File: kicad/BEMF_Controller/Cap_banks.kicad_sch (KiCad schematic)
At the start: 63 parts

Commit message: Simplification, high and low side driven together.
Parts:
- C10, C24, C25, C26, C27, C32, C33, C34, C35, C6, C7, C8: footprint main:CPOL-RADIAL-5MM-10MM -> Capacitor_THT:CP_Radial_D10.0mm_P5.00mm; symbol main-eagle-import:1000UF-RADIAL-5MM-25V-20% -> Component_Library:C_Pol_470uF
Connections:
- net CAP_BANK_A+: now also C10.1; no longer C10.+
- net CAP_BANK_B+: now also C27.1; no longer C27.+
- net CAP_BANK_C+: now also C35.1; no longer C35.+
- net SHUNT_A+: now also C8.2; no longer C8.-
- net SHUNT_B+: now also C26.2; no longer C26.-
- net SHUNT_C+: now also C34.2; no longer C34.-
- net at C30.2, D20.1 (A), D20.2 (A)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: now also C27.2; no longer C27.-
- net at C28.1, D24.1 (A), D24.2 (A)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: now also C25.1; no longer C25.+
- net at C31.2, D21.1 (A), D21.2 (A)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: now also C24.2; no longer C24.-
- net at C13.1, D13.1 (A), D13.2 (A)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: now also C6.1; no longer C6.+
- net at C23.2, D13.3 (K), D8.1 (A)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: now also C10.2; no longer C10.-
- net at C22.1, D15.1 (A), D15.2 (A)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: now also C8.1; no longer C8.+
- net at C29.1, D25.1 (A), D25.2 (A)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: now also C26.1; no longer C26.+
- net at C28.2, D22.1 (A), D22.2 (A)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: now also C25.2; no longer C25.-
- net at C36.1, D34.1 (A), D34.2 (A)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: now also C33.1; no longer C33.+
- net at C36.2, D32.1 (A), D32.2 (A)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: now also C33.2; no longer C33.-
- net at C37.1, D35.1 (A), D35.2 (A)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: now also C34.1; no longer C34.+
- net at C21.2, D12.1 (A), D12.2 (A)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: now also C7.2; no longer C7.-
- net at C38.2, D30.1 (A), D30.2 (A)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: now also C35.2; no longer C35.-
- net at C13.2, D10.1 (A), D10.2 (A)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: now also C6.2; no longer C6.-
- net at C31.1, D23.1 (A), D23.2 (A)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: now also C24.1; no longer C24.+
- net at C39.1, D33.1 (A), D33.2 (A)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: now also C32.1; no longer C32.+
- net at C21.1, D14.1 (A), D14.2 (A)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: now also C7.1; no longer C7.+
- net at C39.2, D31.1 (A), D31.2 (A)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: now also C32.2; no longer C32.-

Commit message: Fixed all warnings.
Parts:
- R30, R31, R32: footprint main:R2512 -> Resistor_SMD:R_2512_6332Metric_Pad1.40x3.35mm_HandSolder; symbol main-eagle-import:RESISTOR -> Component_Library:R0005
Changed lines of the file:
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@@
 	)
 	(junction
-		(at 105.41 175.26)
-		(diameter 0)
-		(color 0 0 0 0)
-	)
-	(junction
 		(at 124.46 157.48)
 		(diameter 0)
@@
 	)
 	(junction
+		(at 30.48 185.42)
+		(diameter 0)
+		(color 0 0 0 0)
+	)
+	(junction
 		(at 143.51 115.57)
 		(diameter 0)
@@
 	)
 	(junction
-		(at 105.41 185.42)
+		(at 30.48 175.26)
 		(diameter 0)
 		(color 0 0 0 0)
@@
 	)
 	(junction
+		(at 105.41 175.26)
+		(diameter 0)
+		(color 0 0 0 0)
+	)
+	(junction
 		(at 196.85 127)
 		(diameter 0)
@@
 	)
 	(junction
-		(at 196.85 36.83)
+		(at 182.88 185.42)
 		(diameter 0)
 		(color 0 0 0 0)
 	)
 	(junction
-		(at 182.88 175.26)
+		(at 196.85 36.83)
 		(diameter 0)
 		(color 0 0 0 0)
@@
 	)
 	(junction
-		(at 30.48 185.42)
+		(at 105.41 185.42)
 		(diameter 0)
 		(color 0 0 0 0)
@@
 	)
 	(junction
-		(at 182.88 185.42)
-		(diameter 0)
-		(color 0 0 0 0)
-	)
-	(junction
-		(at 30.48 175.26)
-		(diameter 0)
-		(color 0 0 0 0)
-	)
-	(junction
 		(at 44.45 60.96)
 		(diameter 0)
@@
 	)
 	(junction
+		(at 182.88 175.26)
+		(diameter 0)
+		(color 0 0 0 0)
+	)
+	(junction
 		(at 196.85 99.06)
 		(diameter 0)
@@
 	(wire
 		(pts
-			(xy 182.88 175.26) (xy 191.77 175.26)
-		)
-		(stroke
-			(width 0)
-			(type default)
-		)
-	)
-	(wire
-		(pts
 			(xy 201.93 77.47) (xy 201.93 81.28)
 		)
@@
 	(wire
 		(pts
-			(xy 30.48 175.26) (xy 39.37 175.26)
+			(xy 30.48 175.26) (xy 30.48 176.53)
 		)
 		(stroke
@@
 	(wire
 		(pts
-			(xy 67.31 157.48) (xy 64.77 157.48)
+			(xy 30.48 184.15) (xy 30.48 185.42)
 		)
 		(stroke
@@
 	(wire
 		(pts
-			(xy 30.48 185.42) (xy 38.1 185.42)
+			(xy 67.31 157.48) (xy 64.77 157.48)
 		)
 		(stroke
@@
 	(wire
 		(pts
-			(xy 182.88 185.42) (xy 190.5 185.42)
+			(xy 97.79 26.67) (xy 110.49 26.67)
 		)
 		(stroke
@@
 	(wire
 		(pts
-			(xy 97.79 26.67) (xy 110.49 26.67)
+			(xy 196.85 60.96) (xy 196.85 64.77)
 		)
 		(stroke
@@
 	(wire
 		(pts
-			(xy 196.85 60.96) (xy 196.85 64.77)
+			(xy 31.75 36.83) (xy 44.45 36.83)
 		)
 		(stroke
@@
 	(wire
 		(pts
-			(xy 31.75 36.83) (xy 44.45 36.83)
+			(xy 196.85 115.57) (xy 200.66 115.57)
 		)
 		(stroke
@@
 	(wire
 		(pts
-			(xy 196.85 115.57) (xy 200.66 115.57)
+			(xy 48.26 157.48) (xy 48.26 161.29)
 		)
 		(stroke
@@
 	(wire
 		(pts
-			(xy 48.26 157.48) (xy 48.26 161.29)
+			(xy 125.73 77.47) (xy 125.73 81.28)
 		)
 		(stroke
@@
 	(wire
 		(pts
-			(xy 125.73 77.47) (xy 125.73 81.28)
+			(xy 105.41 175.26) (xy 115.57 175.26)
 		)
 		(stroke
@@
 	(wire
 		(pts
+			(xy 30.48 175.26) (xy 39.37 175.26)
+		)
+		(stroke
+			(width 0)
+			(type default)
+		)
+	)
+	(wire
+		(pts
 			(xy 54.61 157.48) (xy 57.15 157.48)
 		)
@@
 	(wire
 		(pts
-			(xy 182.88 185.42) (xy 171.45 185.42)
+			(xy 171.45 185.42) (xy 182.88 185.42)
 		)
 		(stroke
@@
 	(wire
 		(pts
+			(xy 182.88 175.26) (xy 191.77 175.26)
+		)
+		(stroke
+			(width 0)
+			(type default)
+		)
+	)
+	(wire
+		(pts
 			(xy 173.99 99.06) (xy 181.61 99.06)
 		)
@@
 	(wire
 		(pts
-			(xy 30.48 185.42) (xy 20.32 185.42)
+			(xy 20.32 185.42) (xy 30.48 185.42)
 		)
 		(stroke
@@
 	(wire
 		(pts
+			(xy 105.41 185.42) (xy 113.03 185.42)
+		)
+		(stroke
+			(width 0)
+			(type default)
+		)
+	)
+	(wire
+		(pts
+			(xy 182.88 185.42) (xy 190.5 185.42)
+		)
+		(stroke
+			(width 0)
+			(type default)
+		)
+	)
+	(wire
+		(pts
 			(xy 116.84 41.91) (xy 116.84 48.26)
 		)
@@
 	(wire
 		(pts
+			(xy 105.41 175.26) (xy 105.41 176.53)
+		)
+		(stroke
+			(width 0)
+			(type default)
+		)
+	)
+	(wire
+		(pts
 			(xy 124.46 157.48) (xy 124.46 161.29)
 		)
@@
 	(wire
 		(pts
-			(xy 105.41 175.26) (xy 115.57 175.26)
-		)
-		(stroke
-			(width 0)
-			(type default)
-		)
-	)
-	(wire
-		(pts
 			(xy 97.79 36.83) (xy 100.33 36.83)
 		)
@@
 	(wire
 		(pts
+			(xy 182.88 184.15) (xy 182.88 185.42)
+		)
+		(stroke
+			(width 0)
+			(type default)
+		)
+	)
+	(wire
+		(pts
 			(xy 55.88 36.83) (xy 44.45 36.83)
 		)
@@
 	(wire
 		(pts
+			(xy 182.88 175.26) (xy 182.88 176.53)
+		)
+		(stroke
+			(width 0)
+			(type default)
+		)
+	)
+	(wire
+		(pts
 			(xy 58.42 147.32) (xy 54.61 147.32)
 		)
@@
 	(wire
 		(pts
+			(xy 105.41 184.15) (xy 105.41 185.42)
+		)
+		(stroke
+			(width 0)
+			(type default)
+		)
+	)
+	(wire
+		(pts
 			(xy 120.65 127) (xy 120.65 137.16)
 		)
@@
 	(wire
 		(pts
+			(xy 30.48 185.42) (xy 38.1 185.42)
+		)
+		(stroke
+			(width 0)
+			(type default)
+		)
+	)
+	(wire
+		(pts
 			(xy 120.65 91.44) (xy 120.65 99.06)
 		)
@@
 	(wire
 		(pts
-			(xy 105.41 185.42) (xy 113.03 185.42)
-		)
-		(stroke
-			(width 0)
-			(type default)
-		)
-	)
-	(wire
-		(pts
 			(xy 115.57 115.57) (xy 115.57 119.38)
 		)
@@
 	)
 	(symbol
-		(lib_id "main-eagle-import:RESISTOR")
-		(at 182.88 180.34 270)
+		(lib_id "Component_Library:R0005")
+		(at 182.88 180.34 0)
 		(unit 1)
 		(exclude_from_sim no)
@@
 		(dnp no)
 		(property "Reference" "R32"
-			(at 184.404 180.34 0)
+			(at 178.308 181.102 0)
 			(effects
 				(font
@@
 		)
 		(property "Value" "0.0005"
-			(at 181.356 180.34 0)
+			(at 189.738 179.07 0)
 			(effects
 				(font
@@
 			)
 		)
-		(property "Footprint" "main:R2512"
-			(at 182.88 180.34 0)
+		(property "Footprint" "Resistor_SMD:R_2512_6332Metric_Pad1.40x3.35mm_HandSolder"
+			(at 181.102 180.34 90)
 			(effects
 				(font
@@
 			)
 		)
-		(property "Datasheet" ""
+		(property "Datasheet" "~"
 			(at 182.88 180.34 0)
 			(effects
@@
 			)
 		)
-		(property "Description" ""
+		(property "Description" "Resistor"
 			(at 182.88 180.34 0)
 			(effects
@@
 	)
 	(symbol
-		(lib_id "main-eagle-import:RESISTOR")
-		(at 105.41 180.34 270)
+		(lib_id "Component_Library:R0005")
+		(at 105.41 180.34 0)
 		(unit 1)
 		(exclude_from_sim no)
@@
 		(dnp no)
 		(property "Reference" "R31"
-			(at 106.934 180.34 0)
+			(at 101.346 180.086 0)
 			(effects
 				(font
@@
 		)
 		(property "Value" "0.0005"
-			(at 103.886 180.34 0)
+			(at 112.522 179.832 0)
 			(effects
 				(font
@@
 			)
 		)
-		(property "Footprint" "main:R2512"
-			(at 105.41 180.34 0)
+		(property "Footprint" "Resistor_SMD:R_2512_6332Metric_Pad1.40x3.35mm_HandSolder"
+			(at 103.632 180.34 90)
 			(effects
 				(font
@@
 			)
 		)
-		(property "Datasheet" ""
+		(property "Datasheet" "~"
 			(at 105.41 180.34 0)
 			(effects
@@
 			)
 		)
-		(property "Description" ""
+		(property "Description" "Resistor"
 			(at 105.41 180.34 0)
 			(effects
@@
 	)
 	(symbol
-		(lib_id "main-eagle-import:RESISTOR")
-		(at 30.48 180.34 270)
+		(lib_id "Component_Library:R0005")
+		(at 30.48 180.34 0)
 		(unit 1)
 		(exclude_from_sim no)
@@
 		(dnp no)
 		(property "Reference" "R30"
-			(at 32.004 180.34 0)
+			(at 26.162 180.594 0)
 			(effects
 				(font
@@
 		)
 		(property "Value" "0.0005"
-			(at 28.956 180.34 0)
+			(at 38.354 179.832 0)
 			(effects
 				(font
@@
 			)
 		)
-		(property "Footprint" "main:R2512"
-			(at 30.48 180.34 0)
+		(property "Footprint" "Resistor_SMD:R_2512_6332Metric_Pad1.40x3.35mm_HandSolder"
+			(at 28.702 180.34 90)
 			(effects
 				(font
@@
 			)
 		)
-		(property "Datasheet" ""
+		(property "Datasheet" "~"
 			(at 30.48 180.34 0)
 			(effects
@@
 			)
 		)
-		(property "Description" ""
+		(property "Description" "Resistor"
 			(at 30.48 180.34 0)
 			(effects

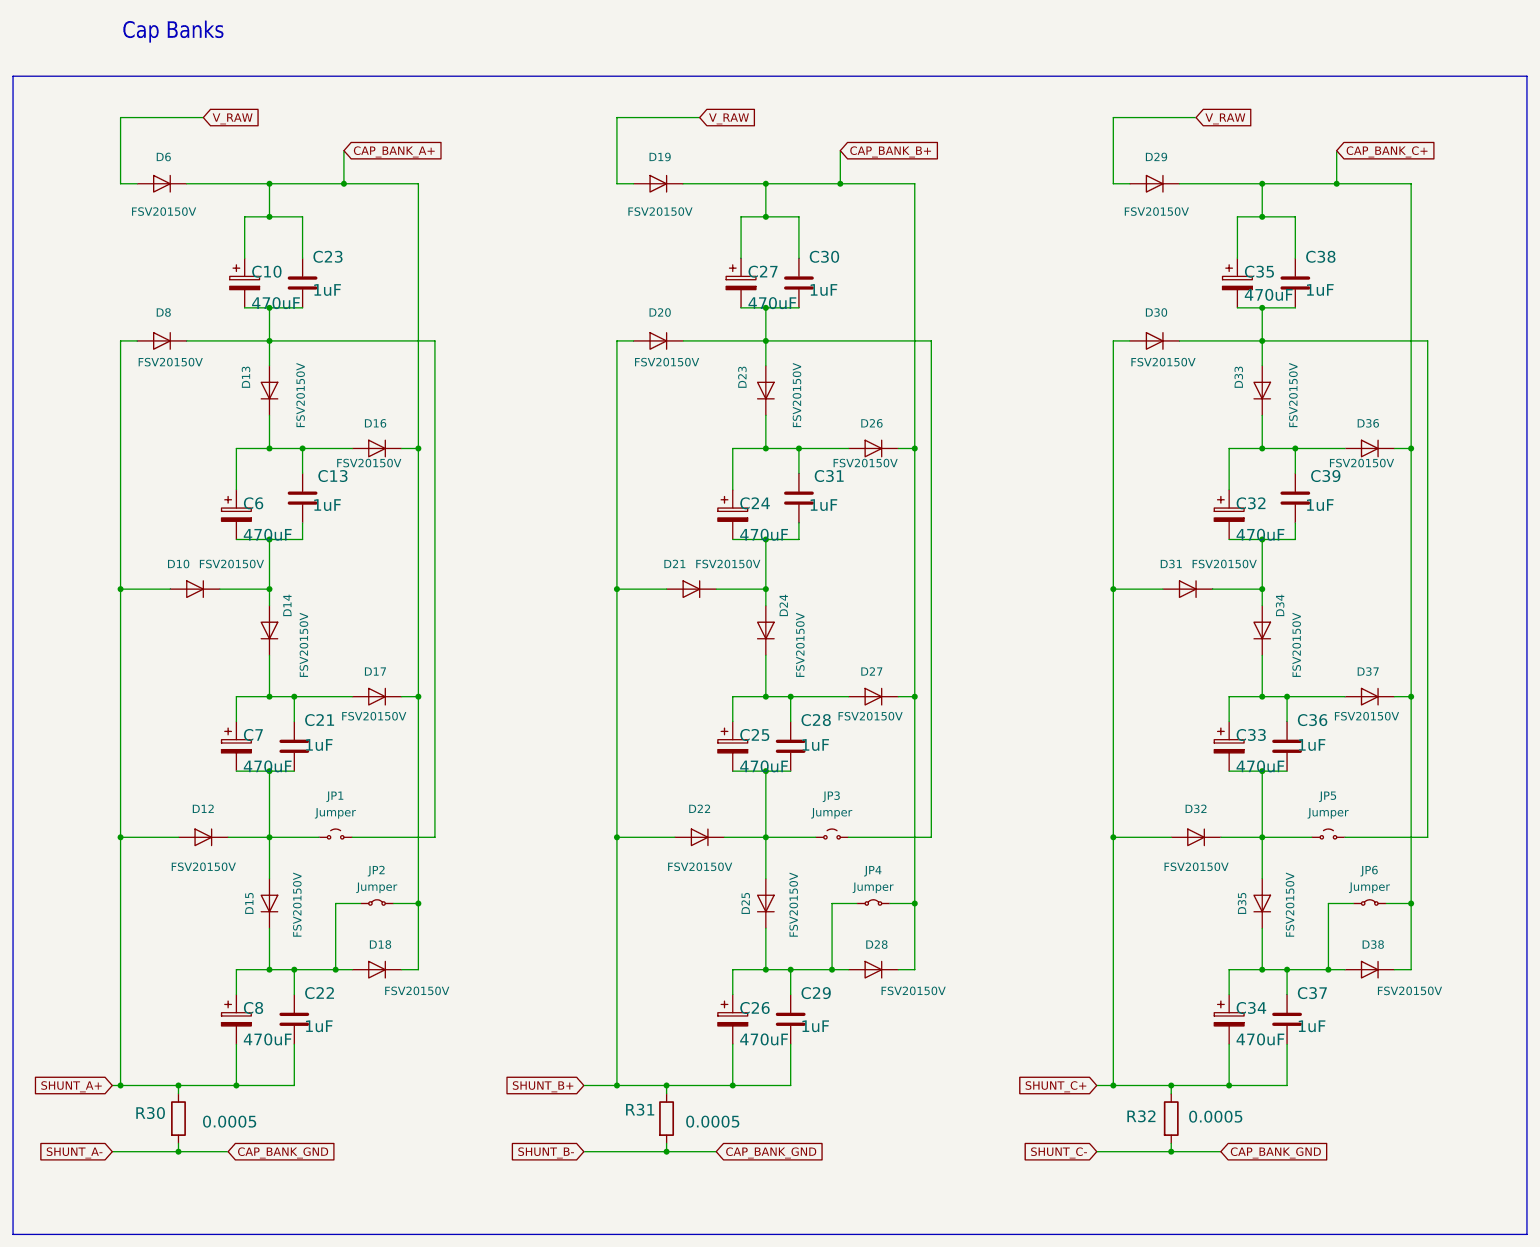
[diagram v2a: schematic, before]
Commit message: Change of plans. Make simple controller for MEG only
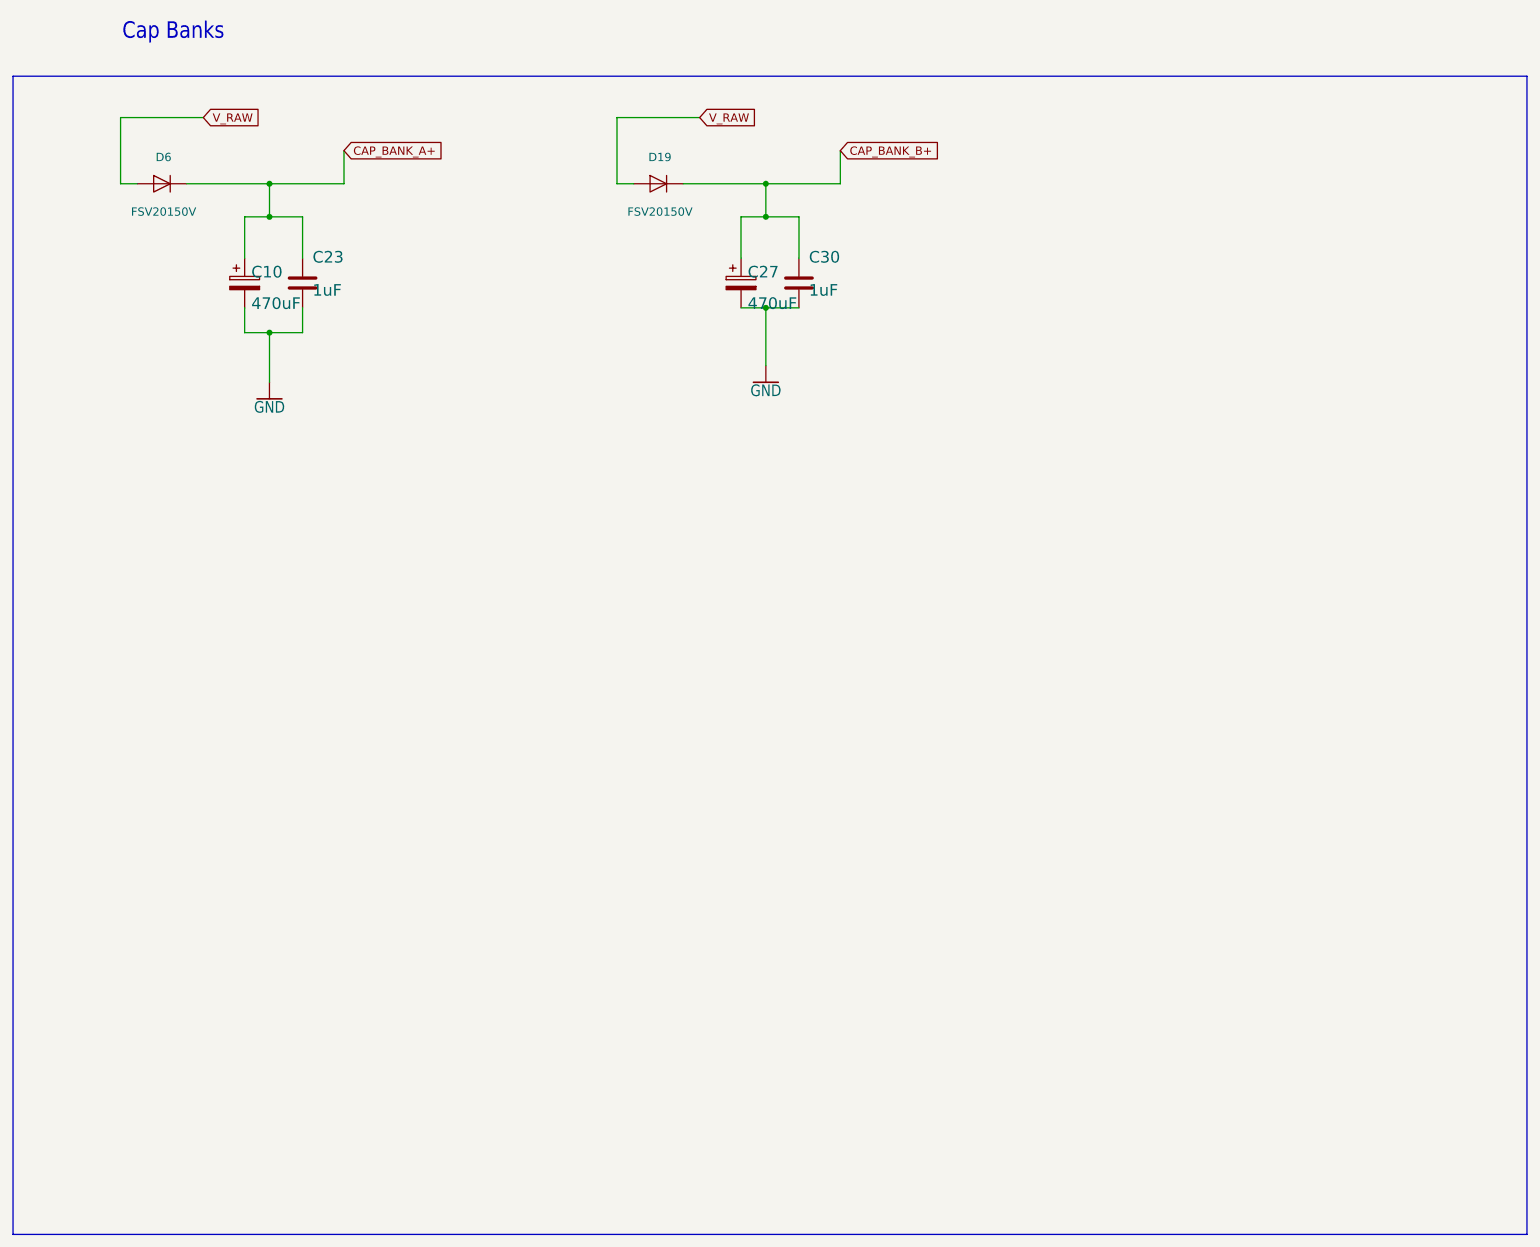
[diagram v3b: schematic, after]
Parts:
- removed C13, C21, C22, C28, C29, C31, C36, C37, C38, C39: 1uF, Capacitor_SMD:C_1812_4532Metric, symbol Component_Library:CHV1812N250105MXT
- removed C24, C25, C26, C32, C33, C34, C35, C6, C7, C8: 470uF, Capacitor_THT:CP_Radial_D10.0mm_P5.00mm, symbol Component_Library:C_Pol_470uF
- removed D10, D12, D13, D14, D15, D16, D17, D18, D20, D21, D22, D23, D24, D25, D26, D27, D28, D29, D30, D31, D32, D33, D34, D35, D36, D37, D38, D8: FSV20150V, Package_TO_SOT_SMD:TO-277A, symbol Component_Library:FSV20150V
- removed JP1, JP3, JP5: Jumper, Jumper:SolderJumper-2_P1.3mm_Open_RoundedPad1.0x1.5mm, symbol Jumper:Jumper_2_Small_Open
- removed JP2, JP4, JP6: Jumper, Jumper:SolderJumper-2_P1.3mm_Bridged2Bar_RoundedPad1.0x1.5mm, symbol Jumper:Jumper_2_Small_Bridged
- removed R30, R31, R32: 0.0005, Resistor_SMD:R_2512_6332Metric_Pad1.40x3.35mm_HandSolder, symbol Component_Library:R0005
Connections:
- net GND: now reaches C27.2, C30.2
- net GND: now also C10.2, C23.2
